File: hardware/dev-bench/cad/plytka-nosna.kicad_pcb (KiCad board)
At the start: 2 copper layers, 170 x 100 mm, 59 parts, among them J1 ARDUINO POWER, J10 CC1120EM P2, J11 ANALIZATOR, J12 VTEST 0-15V, J2 ARDUINO A0-A5, J3 ARDUINO D0-D7, J4 ARDUINO D8-SCL, J5 DEVKITC J1, J6 DEVKITC J3, J7 SHARP 4694, J8 FRAM 4719, J9 CC1120EM P1, Q1 MMBT3904, SW1 GÓRA, SW2 DÓŁ, SW3 OK, SW4 WSTECZ, SW5 CISZA, SW6 PRZYGOTOWANIE

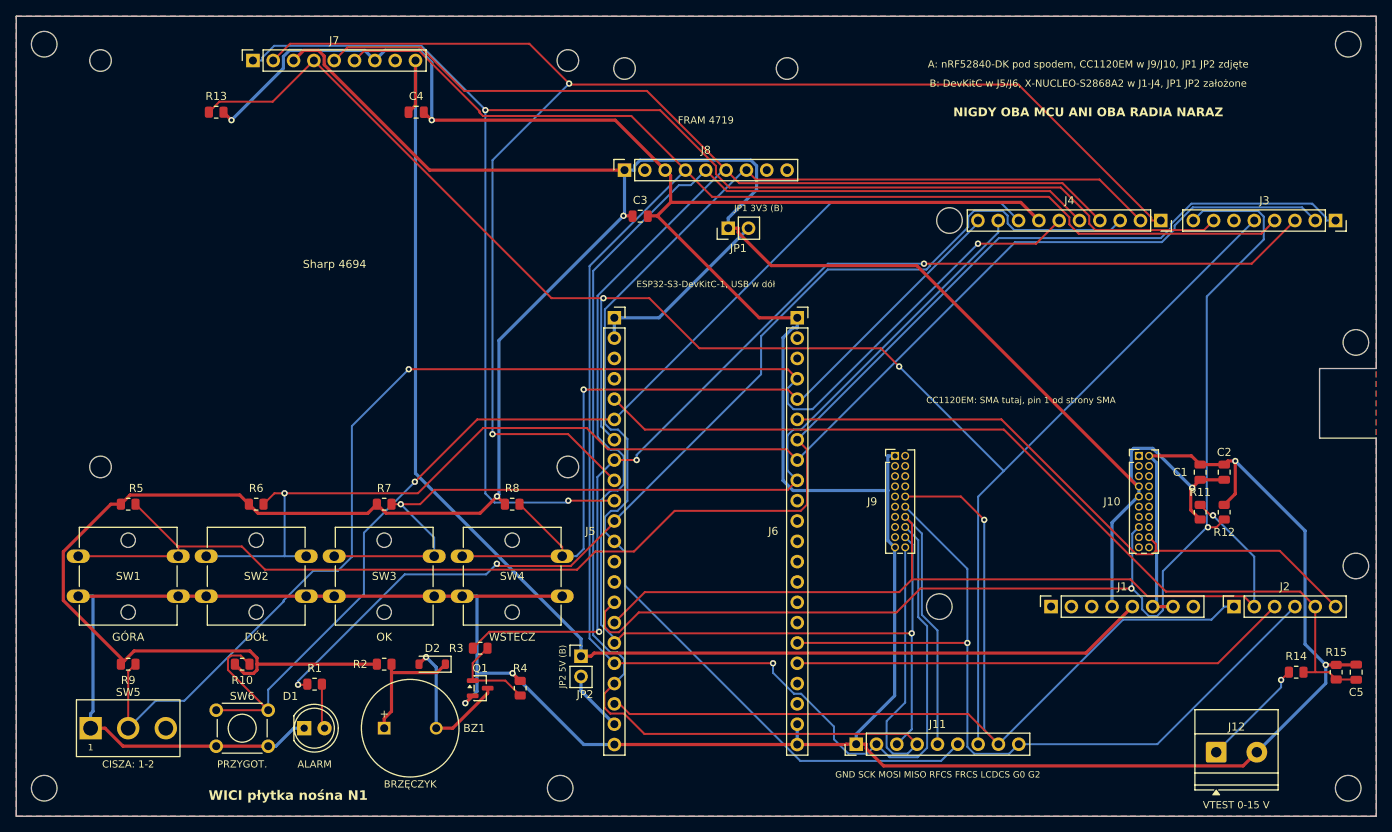
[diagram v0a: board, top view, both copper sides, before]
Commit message: Dev bench: carrier N1 after review, fabrication files for a test build
Review of N1 (electrical, mechanical, docs) found no critical defect;
fixes applied in the generators:
- buzzer from +5V through 22 ohm 1206, not from the radio's 3.0 V rail
- 1k in series with the CISZA switch, 33 ohm series on SCK at both MCUs,
  2k2 pull-down on LCD_DISP, BAT54S clamp on VTEST, RF_RESET pull-down 10k
- JP3 feeds the CC1120EM (radio current measurement in bench A)
- RF_GPIO2 on ESP32 GPIO4 instead of GPIO47 (N16R16V modules fit)
- no copper on B.Cu and no vias over the DK P20 pin row, no tracks under
  standoffs and screw heads, wider P5 notch
- module outlines, SMA circle and USB mark on the silkscreen, text >=1 mm,
  J12 polarity, missing_courtyard check enabled, hole/via minima 0.4/0.8 mm
- BOM: one Adafruit 85 kit, per-part notes, shunts, caps, standoffs

ERC 0, DRC 0, 0 unconnected, 0 schematic parity. Reproduction checked with
tools/compare_boards.py (checks/odtworzenie.md). Fabrication package in
fabrication/N1, schematic PDF, assembly and bring-up procedure, list of
conditions before an order. Docs: F81 updated, R02 no longer called the
first printed board, dev-bench README on wires vs carrier.
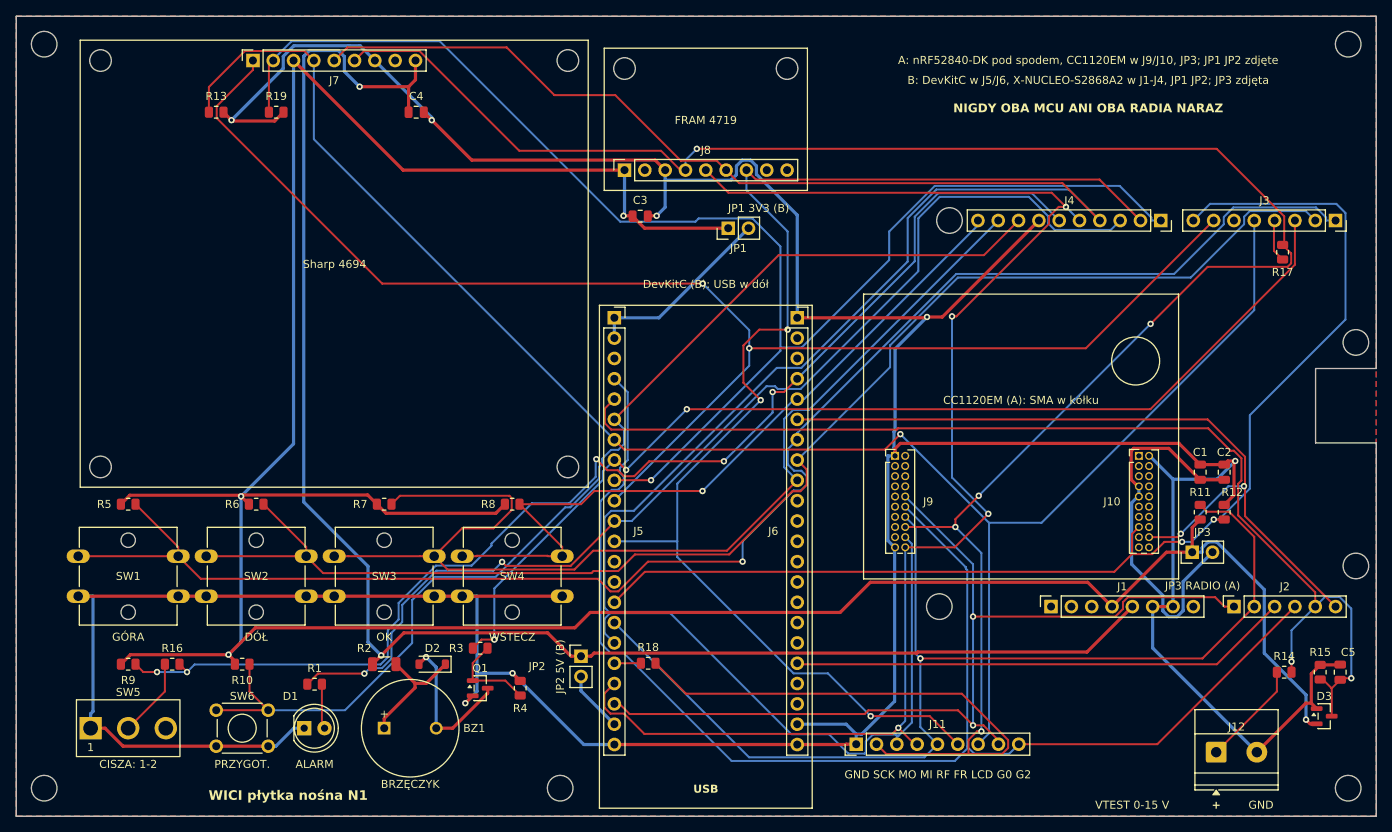
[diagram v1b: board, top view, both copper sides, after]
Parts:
- added D3: BAT54S, Package_TO_SOT_SMD:SOT-23, F.Cu at (193.5, 117.5)
- added JP3: 3V3 RADIO A, Connector_PinHeader_2.54mm:PinHeader_1x02_P2.54mm_Vertical, F.Cu at (177.0, 97.0)
- added R16: 1k, Resistor_SMD:R_0805_2012Metric, F.Cu at (49.5, 111.0)
- added R17: 33R, Resistor_SMD:R_0805_2012Metric, F.Cu at (188.3, 59.5)
- added R18: 33R, Resistor_SMD:R_0805_2012Metric, F.Cu at (109.0, 110.9)
- added R19: 2k2, Resistor_SMD:R_0805_2012Metric, F.Cu at (62.5, 42.0)
- R12: value 100k -> 10k
- R2: value 10R -> 22R; footprint Resistor_SMD:R_0805_2012Metric -> Resistor_SMD:R_1206_3216Metric
- moved C5 2.00 mm to (195.5, 112.0)
- moved R15 2.00 mm to (193.0, 112.0)
- moved R14 1.50 mm to (188.5, 112.0)
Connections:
- C1 pad 1: /+3V3 -> /+3V3_RF
- C2 pad 1: /+3V3 -> /+3V3_RF
- J10 pad 7: /+3V3 -> /+3V3_RF
- J10 pad 9: /+3V3 -> /+3V3_RF
- J3 pad 4: /SPI_SCK -> /SPI_SCK_DK
- J5 pad 18: /SPI_SCK -> /SPI_SCK_DEVKIT
- J5 pad 4: unconnected-(J5-Pin_4-Pad4) -> /RF_GPIO2
- J6 pad 17: /RF_GPIO2 -> unconnected-(J6-Pin_17-Pad17)
- R2 pad 1: /+3V3 -> /+5V
- SW5 pad 2: /SW_CISZA -> /SW_COM
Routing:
- net /RF_GPIO2: track 103.4 -> 170.9 mm, vias 1 -> 0
- net /+3V3_RF: track 0.00 -> 47.9 mm
- net /+5V: track 161.3 -> 202.5 mm, vias 0 -> 2
- net /SPI_MOSI: track 240.3 -> 277.9 mm, vias 1 -> 0
- net /+3V3: track 345.4 -> 376.1 mm, vias 3 -> 4
- net /VTEST: track 113.5 -> 139.8 mm, vias 0 -> 2
- net /GND: track 544.9 -> 520.4 mm, vias 6 -> 7
- net /SPI_SCK: track 270.0 -> 294.1 mm, vias 1 -> 5
- net /SPI_MISO: track 197.9 -> 176.5 mm, vias 0 -> 4
- net /BTN_OK: track 117.2 -> 137.7 mm, vias 1 -> 0
- net /LCD_EXTCOMIN: track 196.9 -> 179.6 mm
- net /RF_GPIO3: track 79.4 -> 96.0 mm, vias 0 -> 2
- net /SW_CISZA: track 168.3 -> 154.6 mm, vias 2 -> 5
- net /SW_COM: track 0.00 -> 9.90 mm
- net /BTN_BACK: track 103.4 -> 93.6 mm
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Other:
- outline, holes or cut-outs redrawn
- board text added: "+"
- board text added: "A: nRF52840-DK pod spodem, CC1120EM w J9/J10, JP3; JP1 JP2 zdjęte"
- board text added: "B: DevKitC w J5/J6, X-NUCLEO-S2868A2 w J1-J4, JP1 JP2; JP3 zdjęta"
- board text added: "CC1120EM (A): SMA w kółku"
- board text added: "DevKitC (B): USB w dół"
- board text added: "GND"
- board text added: "GND SCK MO MI RF FR LCD G0 G2"
- board text added: "JP3 RADIO (A)"
- board text added: "USB"
- board text added: "skala: 50 mm przy wydruku 1:1"
- board text removed: "A: nRF52840-DK pod spodem, CC1120EM w J9/J10, JP1 JP2 zdjęte"
- board text removed: "B: DevKitC w J5/J6, X-NUCLEO-S2868A2 w J1-J4, JP1 JP2 założone"
- board text removed: "CC1120EM: SMA tutaj, pin 1 od strony SMA"
- board text removed: "ESP32-S3-DevKitC-1, USB w dół"
- board text removed: "GND SCK MOSI MISO RFCS FRCS LCDCS G0 G2"
